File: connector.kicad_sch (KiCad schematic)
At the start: 1 part, among them J4 Conn_02x13_Row_Letter_Last

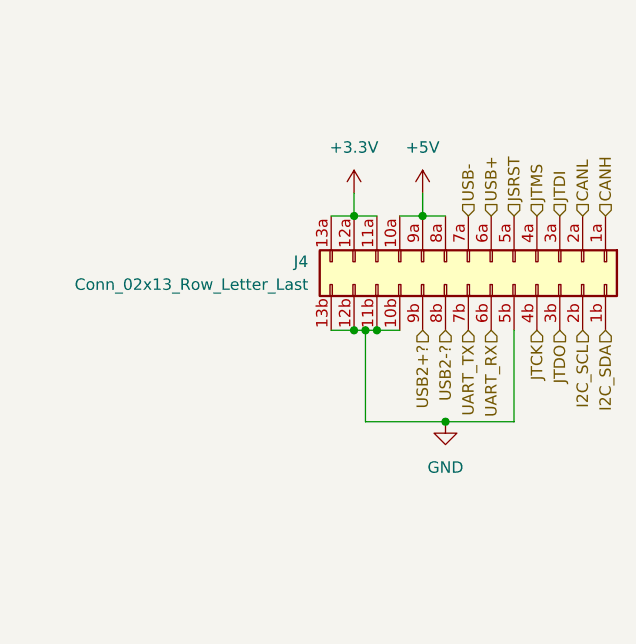
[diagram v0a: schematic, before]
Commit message: 3.3V changes and changed labels to hierarchical one's
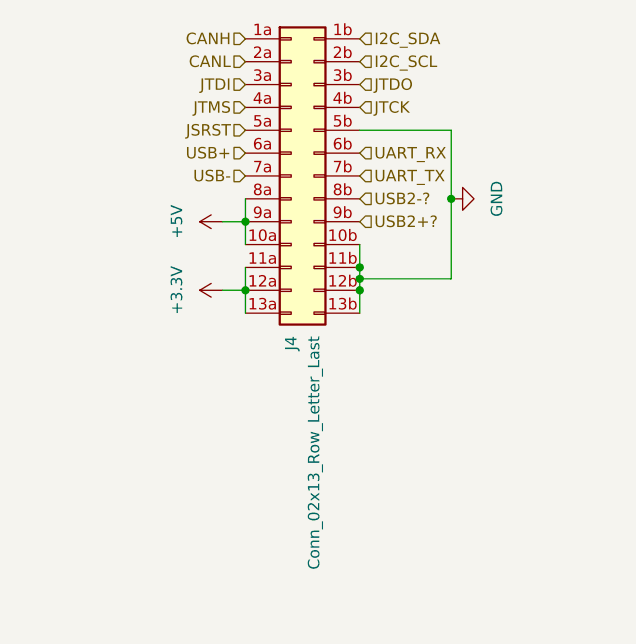
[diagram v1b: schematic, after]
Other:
- moved on the sheet: J4

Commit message: linked everything together. still need to add capacitors
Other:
- moved on the sheet: J4
